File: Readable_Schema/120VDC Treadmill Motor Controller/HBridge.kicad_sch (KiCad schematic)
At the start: 71 parts, among them J2 OSTT7020150, Q1 IPP60R060P7XKSA1, Q2 IPP60R060P7XKSA1, Q3 IPP60R060P7XKSA1, Q4 IPP60R060P7XKSA1, U1 UCC21530DWKR, U2 UCC21530DWKR

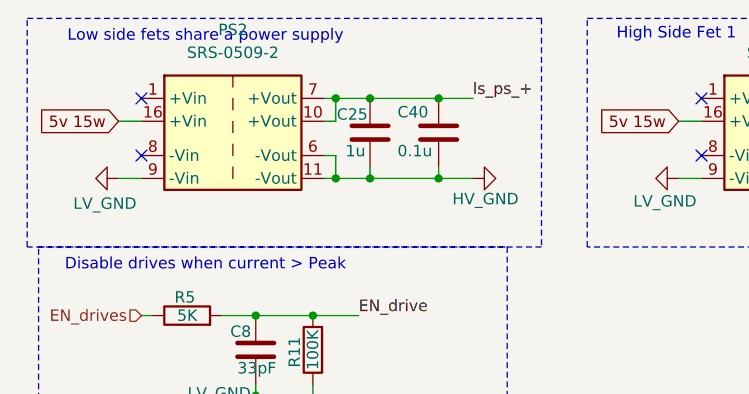
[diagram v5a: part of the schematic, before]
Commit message: -Still working on traces, working through mostly traces on the low voltage side rather than HV pours like before.
-I'm sure there's a real strategy to these LV traces but I'm not really aware of what that is.

-Will need to go back and clean up a the pours on the HV side
--Add fillets
--proper spacing within same layer
--More room around fet pins to not bottleneck current
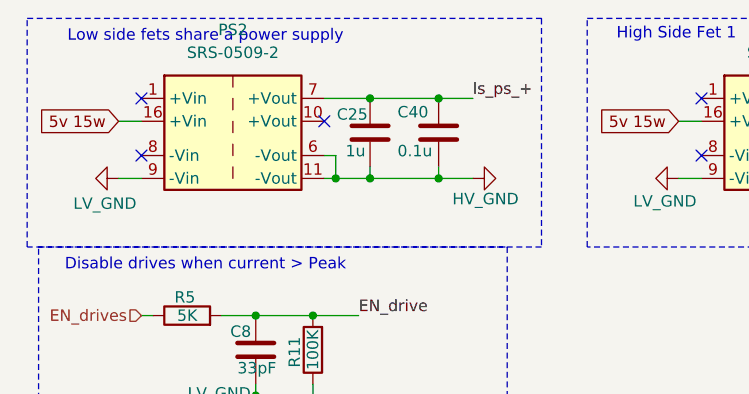
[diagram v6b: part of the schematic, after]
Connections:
- net ls_ps_+: no longer PS2.10 (+Vout)
- no-connect marks 14 -> 15
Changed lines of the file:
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@@
-	)
-	(junction
-		(at 45.72 21.59)
-		(diameter 0)
-		(color 0 0 0 0)
 	)
 	(junction
@@
 	)
 	(no_connect
+		(at 44.45 24.13)
+	)
+	(no_connect
 		(at 24.13 27.94)
 	)
@@
 	(wire
 		(pts
-			(xy 45.72 24.13) (xy 45.72 21.59)
-		)
-		(stroke
-			(width 0)
-			(type default)
-		)
-	)
-	(wire
-		(pts
 			(xy 120.65 21.59) (xy 124.46 21.59)
 		)
@@
 	(wire
 		(pts
-			(xy 44.45 21.59) (xy 45.72 21.59)
-		)
-		(stroke
-			(width 0)
-			(type default)
-		)
-	)
-	(wire
-		(pts
 			(xy 27.94 101.6) (xy 27.94 105.41)
 		)
@@
 	(wire
 		(pts
-			(xy 44.45 24.13) (xy 45.72 24.13)
-		)
-		(stroke
-			(width 0)
-			(type default)
-		)
-	)
-	(wire
-		(pts
 			(xy 233.68 116.84) (xy 233.68 129.54)
 		)
@@
 	(wire
 		(pts
-			(xy 45.72 21.59) (xy 49.53 21.59)
-		)
-		(stroke
+			(xy 44.45 21.59) (xy 49.53 21.59)
+		)
+		(stroke

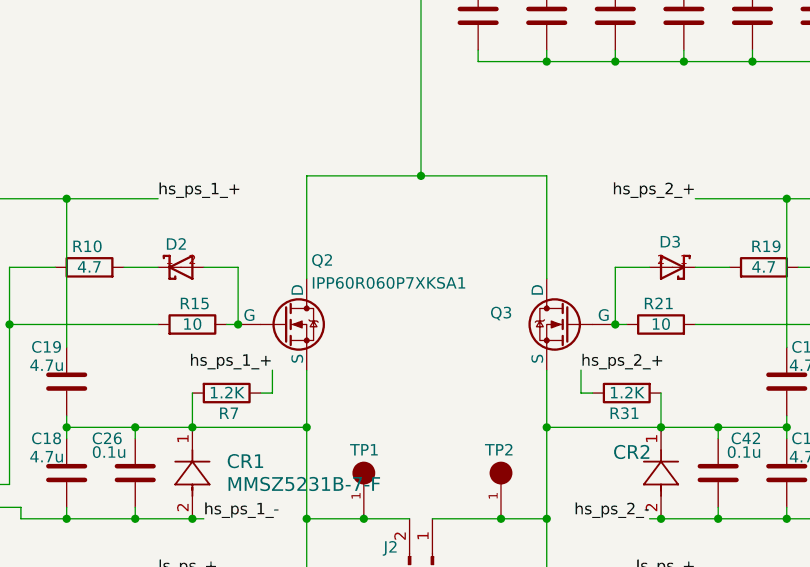
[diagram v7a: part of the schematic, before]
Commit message: Need to check fet, caps, connector footprints (and cap discharge) on power subcircuit. Currently working through checking all footprints to hopefully save a major headache if there is a mistake
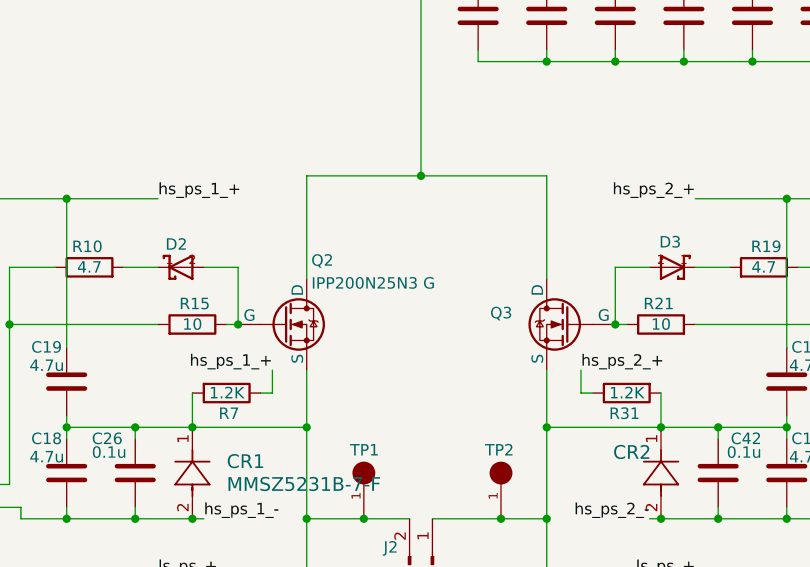
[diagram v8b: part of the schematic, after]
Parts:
- Q1, Q2, Q3, Q4: value IPP60R060P7XKSA1 -> IPP200N25N3 G
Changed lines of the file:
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@@
 			)
 		)
-		(property "Value" "IPP60R060P7XKSA1"
+		(property "Value" "IPP200N25N3 G"
 			(at 157.48 90.1699 0)
 			(effects
@@
 			)
 		)
-		(property "Datasheet" "https://www.infineon.com/dgdl/Infineon-IPP60R060P7-DS-v02_00-EN.pdf?fileId=5546d4625acbae4c015accdf20660227"
+		(property "Datasheet" "https://www.infineon.com/assets/row/public/documents/24/49/infineon-ipp-b-i-200n25n3-g-datasheet-en.pdf?folderId=db3a3043163797a6011637d4bae7003b&fileId=db3a3043243b5f17012496b87e9f1971"
 			(at 163.83 101.6 0)
 			(effects
@@
 		)
 		(instances
-			(project ""
+			(project "120VDC Treadmill Motor Controller"
 				(path "/319bc5c0-2dd5-4df3-a34b-9170833ebccd/49a5a11b-8174-445d-b343-1fe5ec8c60de"
 					(reference "CR1")
@@
 		)
 		(instances
-			(project ""
+			(project "120VDC Treadmill Motor Controller"
 				(path "/319bc5c0-2dd5-4df3-a34b-9170833ebccd/49a5a11b-8174-445d-b343-1fe5ec8c60de"
 					(reference "C28")
@@
 		)
 		(instances
-			(project ""
+			(project "120VDC Treadmill Motor Controller"
 				(path "/319bc5c0-2dd5-4df3-a34b-9170833ebccd/49a5a11b-8174-445d-b343-1fe5ec8c60de"
 					(reference "U2")
@@
 			)
 		)
-		(property "Value" "IPP60R060P7XKSA1"
+		(property "Value" "IPP200N25N3 G"
 			(at 135.128 84.328 0)
 			(effects
@@
 			)
 		)
-		(property "Datasheet" "https://www.infineon.com/dgdl/Infineon-IPP60R060P7-DS-v02_00-EN.pdf?fileId=5546d4625acbae4c015accdf20660227"
+		(property "Datasheet" "https://www.infineon.com/assets/row/public/documents/24/49/infineon-ipp-b-i-200n25n3-g-datasheet-en.pdf?folderId=db3a3043163797a6011637d4bae7003b&fileId=db3a3043243b5f17012496b87e9f1971"
 			(at 132.08 101.6 0)
 			(effects
@@
 		)
 		(instances
-			(project ""
+			(project "120VDC Treadmill Motor Controller"
 				(path "/319bc5c0-2dd5-4df3-a34b-9170833ebccd/49a5a11b-8174-445d-b343-1fe5ec8c60de"
 					(reference "Q2")
@@
 		)
 		(instances
-			(project ""
+			(project "120VDC Treadmill Motor Controller"
 				(path "/319bc5c0-2dd5-4df3-a34b-9170833ebccd/49a5a11b-8174-445d-b343-1fe5ec8c60de"
 					(reference "#PWR010")
@@
 		)
 		(instances
-			(project ""
+			(project "120VDC Treadmill Motor Controller"
 				(path "/319bc5c0-2dd5-4df3-a34b-9170833ebccd/49a5a11b-8174-445d-b343-1fe5ec8c60de"
 					(reference "D2")
@@
 		)
 		(instances
-			(project ""
+			(project "120VDC Treadmill Motor Controller"
 				(path "/319bc5c0-2dd5-4df3-a34b-9170833ebccd/49a5a11b-8174-445d-b343-1fe5ec8c60de"
 					(reference "TP1")
@@
 			)
 		)
-		(property "Value" "IPP60R060P7XKSA1"
+		(property "Value" "IPP200N25N3 G"
 			(at 157.48 123.1899 0)
 			(effects
@@
 			)
 		)
-		(property "Datasheet" "https://www.infineon.com/dgdl/Infineon-IPP60R060P7-DS-v02_00-EN.pdf?fileId=5546d4625acbae4c015accdf20660227"
+		(property "Datasheet" "https://www.infineon.com/assets/row/public/documents/24/49/infineon-ipp-b-i-200n25n3-g-datasheet-en.pdf?folderId=db3a3043163797a6011637d4bae7003b&fileId=db3a3043243b5f17012496b87e9f1971"
 			(at 163.83 134.62 0)
 			(effects
@@
 			)
 		)
-		(property "Value" "IPP60R060P7XKSA1"
+		(property "Value" "IPP200N25N3 G"
 			(at 138.43 123.1899 0)
 			(effects
@@
 			)
 		)
-		(property "Datasheet" "https://www.infineon.com/dgdl/Infineon-IPP60R060P7-DS-v02_00-EN.pdf?fileId=5546d4625acbae4c015accdf20660227"
+		(property "Datasheet" "https://www.infineon.com/assets/row/public/documents/24/49/infineon-ipp-b-i-200n25n3-g-datasheet-en.pdf?folderId=db3a3043163797a6011637d4bae7003b&fileId=db3a3043243b5f17012496b87e9f1971"
 			(at 132.08 134.62 0)
 			(effects
@@
 		)
 		(instances
-			(project ""
+			(project "120VDC Treadmill Motor Controller"
 				(path "/319bc5c0-2dd5-4df3-a34b-9170833ebccd/49a5a11b-8174-445d-b343-1fe5ec8c60de"
 					(reference "R2")
